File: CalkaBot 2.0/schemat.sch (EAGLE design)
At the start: 55 parts, among them IC1 TB6612FNG, IC2 LM339D, IC3 7806DT, Q1 16MHz, X1 MINI-USB-32005-301

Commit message: zmiana przycisków
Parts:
- removed BUT1, BUT2, BUT3: (no value), switch-omron:10-XX
- added SW2: (no value), special:SW_DIP-3
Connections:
- net GND: now also SW2.1, SW2.2, SW2.3; no longer BUT1.S, BUT1.S1, BUT2.S, BUT2.S1, BUT3.S, BUT3.S1
- net MISO: now also SW2.4; no longer BUT1.P, BUT1.P1
- net MOSI: now also SW2.5; no longer BUT2.P, BUT2.P1
- net SCK: now also SW2.6; no longer BUT3.P, BUT3.P1
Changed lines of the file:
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@@
 <?xml version="1.0" encoding="utf-8"?>
 <!DOCTYPE eagle SYSTEM "eagle.dtd">
-<eagle version="8.6.0">
+<eagle version="9.1.3">
 <drawing>
 <settings>
@@
 <part name="GND4" library="supply1" library_urn="urn:adsk.eagle:library:371" deviceset="GND" device=""/>
 <part name="R2" library="rcl" library_urn="urn:adsk.eagle:library:334" deviceset="R-EU_" device="R0805" package3d_urn="urn:adsk.eagle:package:23553/2" value="10k"/>
-<part name="BUT1" library="switch-omron" library_urn="urn:adsk.eagle:library:377" deviceset="10-XX" device="" package3d_urn="urn:adsk.eagle:package:27496/1"/>
 <part name="X1" library="con-cypressindustries" library_urn="urn:adsk.eagle:library:138" deviceset="MINI-USB-" device="32005-301" package3d_urn="urn:adsk.eagle:package:6446/1"/>
 <part name="R6" library="rcl" library_urn="urn:adsk.eagle:library:334" deviceset="R-EU_" device="R0805" package3d_urn="urn:adsk.eagle:package:23553/2" value="10k"/>
-<part name="BUT2" library="switch-omron" library_urn="urn:adsk.eagle:library:377" deviceset="10-XX" device="" package3d_urn="urn:adsk.eagle:package:27496/1"/>
 <part name="R9" library="rcl" library_urn="urn:adsk.eagle:library:334" deviceset="R-EU_" device="R0805" package3d_urn="urn:adsk.eagle:package:23553/2" value="10k"/>
-<part name="BUT3" library="switch-omron" library_urn="urn:adsk.eagle:library:377" deviceset="10-XX" device="" package3d_urn="urn:adsk.eagle:package:27496/1"/>
 <part name="IC3" library="linear3" deviceset="78*" device="DT" technology="06"/>
 <part name="GND7" library="supply1" library_urn="urn:adsk.eagle:library:371" deviceset="GND" device=""/>
@@
 <part name="JP2" library="pinhead" library_urn="urn:adsk.eagle:library:325" deviceset="PINHD-1X5" device="" package3d_urn="urn:adsk.eagle:package:22469/2"/>
 <part name="JP3" library="pinhead" library_urn="urn:adsk.eagle:library:325" deviceset="PINHD-1X5" device="" package3d_urn="urn:adsk.eagle:package:22469/2"/>
+<part name="SW2" library="special" library_urn="urn:adsk.eagle:library:367" deviceset="SW_DIP-3" device="" package3d_urn="urn:adsk.eagle:package:26663/2"/>
+<part name="GND22" library="supply1" library_urn="urn:adsk.eagle:library:371" deviceset="GND" device=""/>
 </parts>
 <sheets>
@@
 <instance part="GND4" gate="1" x="70.866" y="69.85"/>
 <instance part="R2" gate="G$1" x="-88.138" y="-0.508"/>
-<instance part="BUT1" gate="1" x="-88" y="-10.26" rot="R90"/>
 <instance part="X1" gate="G$1" x="-149.86" y="43.18" rot="R180"/>
 <instance part="R6" gate="G$1" x="-34.798" y="-0.508"/>
-<instance part="BUT2" gate="1" x="-34.66" y="-10.26" rot="R90"/>
 <instance part="R9" gate="G$1" x="21.082" y="-0.508"/>
-<instance part="BUT3" gate="1" x="21.22" y="-10.26" rot="R90"/>
 <instance part="IC3" gate="A1" x="68.58" y="124.46"/>
 <instance part="GND7" gate="1" x="68.58" y="111.76"/>
@@
 <instance part="JP2" gate="A" x="-119.38" y="25.4" rot="R270"/>
 <instance part="JP3" gate="A" x="-119.38" y="15.24" rot="R270"/>
+<instance part="SW2" gate="A" x="-27.94" y="-17.78" rot="R270"/>
+<instance part="GND22" gate="1" x="-27.94" y="-27.94"/>
 </instances>
 <busses>
@@
 <bus name="B$3">
 <segment>
-<wire x1="-111.76" y1="7.62" x2="-111.76" y2="-20.32" width="0.762" layer="92" style="shortdash"/>
-<wire x1="-111.76" y1="-20.32" x2="60.96" y2="-20.32" width="0.762" layer="92" style="shortdash"/>
-<wire x1="60.96" y1="-20.32" x2="60.96" y2="7.62" width="0.762" layer="92" style="shortdash"/>
+<wire x1="-111.76" y1="7.62" x2="-111.76" y2="-35.56" width="0.762" layer="92" style="shortdash"/>
+<wire x1="-111.76" y1="-35.56" x2="60.96" y2="-35.56" width="0.762" layer="92" style="shortdash"/>
+<wire x1="60.96" y1="-35.56" x2="60.96" y2="7.62" width="0.762" layer="92" style="shortdash"/>
 <wire x1="60.96" y1="7.62" x2="-111.76" y2="7.62" width="0.762" layer="92" style="shortdash"/>
 </segment>
@@
 </segment>
 <segment>
-<wire x1="-93.08" y1="-5.334" x2="-103.632" y2="-5.334" width="0.1524" layer="91"/>
-<junction x="-103.632" y="-5.334"/>
-<pinref part="BUT1" gate="1" pin="S"/>
-<pinref part="BUT1" gate="1" pin="S1"/>
-<wire x1="-93.08" y1="-10.26" x2="-93.08" y2="-7.72" width="0.1524" layer="91"/>
-<wire x1="-93.08" y1="-7.72" x2="-93.08" y2="-5.334" width="0.1524" layer="91"/>
-<junction x="-93.08" y="-7.72"/>
-<label x="-106.68" y="-5.08" size="1.016" layer="95"/>
-</segment>
-<segment>
 <pinref part="IC3" gate="A1" pin="GND"/>
 <wire x1="68.58" y1="116.84" x2="68.58" y2="114.3" width="0.1524" layer="91"/>
@@
 <wire x1="55.88" y1="137.16" x2="55.88" y2="132.08" width="0.1524" layer="91"/>
 <pinref part="GND18" gate="1" pin="GND"/>
-</segment>
-<segment>
-<wire x1="16.14" y1="-5.334" x2="5.588" y2="-5.334" width="0.1524" layer="91"/>
-<junction x="5.588" y="-5.334"/>
-<pinref part="BUT3" gate="1" pin="S"/>
-<pinref part="BUT3" gate="1" pin="S1"/>
-<wire x1="16.14" y1="-10.26" x2="16.14" y2="-7.72" width="0.1524" layer="91"/>
-<wire x1="16.14" y1="-7.72" x2="16.14" y2="-5.334" width="0.1524" layer="91"/>
-<junction x="16.14" y="-7.72"/>
-<label x="5.08" y="-5.08" size="1.016" layer="95"/>
-</segment>
-<segment>
-<wire x1="-39.74" y1="-5.334" x2="-50.292" y2="-5.334" width="0.1524" layer="91"/>
-<junction x="-50.292" y="-5.334"/>
-<pinref part="BUT2" gate="1" pin="S"/>
-<pinref part="BUT2" gate="1" pin="S1"/>
-<wire x1="-39.74" y1="-10.26" x2="-39.74" y2="-7.72" width="0.1524" layer="91"/>
-<wire x1="-39.74" y1="-7.72" x2="-39.74" y2="-5.334" width="0.1524" layer="91"/>
-<junction x="-39.74" y="-7.72"/>
-<label x="-53.34" y="-5.08" size="1.016" layer="95"/>
 </segment>
 <segment>
@@
 <label x="-46" y="44.5" size="1.778" layer="95"/>
 </segment>
+<segment>
+<pinref part="SW2" gate="A" pin="1"/>
+<pinref part="SW2" gate="A" pin="2"/>
+<wire x1="-30.48" y1="-25.4" x2="-27.94" y2="-25.4" width="0.1524" layer="91"/>
+<pinref part="SW2" gate="A" pin="3"/>
+<wire x1="-25.4" y1="-25.4" x2="-27.94" y2="-25.4" width="0.1524" layer="91"/>
+<junction x="-27.94" y="-25.4"/>
+<pinref part="GND22" gate="1" pin="GND"/>
+</segment>
 </net>
 <net name="D-" class="0">
@@
 <wire x1="-83.058" y1="-0.508" x2="-66.548" y2="-0.508" width="0.1524" layer="91"/>
 <junction x="-66.548" y="-0.508"/>
+<label x="-66.04" y="0" size="1.778" layer="95" xref="yes"/>
+<wire x1="-83.058" y1="-0.508" x2="-83.058" y2="-7.62" width="0.1524" layer="91"/>
+<wire x1="-83.058" y1="-7.62" x2="-33.02" y2="-7.62" width="0.1524" layer="91"/>
 <junction x="-83.058" y="-0.508"/>
-<wire x1="-83.058" y1="-5.334" x2="-83.058" y2="-0.508" width="0.1524" layer="91"/>
-<pinref part="BUT1" gate="1" pin="P1"/>
-<wire x1="-82.92" y1="-7.72" x2="-82.92" y2="-5.334" width="0.1524" layer="91"/>
-<wire x1="-82.92" y1="-5.334" x2="-83.058" y2="-5.334" width="0.1524" layer="91"/>
-<pinref part="BUT1" gate="1" pin="P"/>
-<wire x1="-82.92" y1="-10.26" x2="-82.92" y2="-7.72" width="0.1524" layer="91"/>
-<junction x="-82.92" y="-7.72"/>
-<label x="-66.04" y="0" size="1.778" layer="95" xref="yes"/>
+<pinref part="SW2" gate="A" pin="4"/>
+<wire x1="-33.02" y1="-7.62" x2="-30.48" y2="-7.62" width="0.1524" layer="91"/>
+<wire x1="-25.4" y1="-10.16" x2="-25.4" y2="-7.62" width="0.1524" layer="91"/>
+<wire x1="-25.4" y1="-7.62" x2="-30.48" y2="-7.62" width="0.1524" layer="91"/>
 </segment>
 </net>
@@
 <wire x1="-29.718" y1="-0.508" x2="-13.208" y2="-0.508" width="0.1524" layer="91"/>
 <junction x="-13.208" y="-0.508"/>
+<label x="-12.7" y="0" size="1.778" layer="95" xref="yes"/>
 <junction x="-29.718" y="-0.508"/>
-<wire x1="-29.718" y1="-5.334" x2="-29.718" y2="-0.508" width="0.1524" layer="91"/>
-<pinref part="BUT2" gate="1" pin="P1"/>
-<wire x1="-29.58" y1="-7.72" x2="-29.58" y2="-5.334" width="0.1524" layer="91"/>
-<wire x1="-29.58" y1="-5.334" x2="-29.718" y2="-5.334" width="0.1524" layer="91"/>
-<pinref part="BUT2" gate="1" pin="P"/>
-<wire x1="-29.58" y1="-10.26" x2="-29.58" y2="-7.72" width="0.1524" layer="91"/>
-<junction x="-29.58" y="-7.72"/>
-<label x="-12.7" y="0" size="1.778" layer="95" xref="yes"/>
+<pinref part="SW2" gate="A" pin="5"/>
+<wire x1="-29.718" y1="-0.508" x2="-27.94" y2="-0.508" width="0.1524" layer="91"/>
+<wire x1="-27.94" y1="-0.508" x2="-27.94" y2="-10.16" width="0.1524" layer="91"/>
 </segment>
 </net>
@@
 <wire x1="26.162" y1="-0.508" x2="42.672" y2="-0.508" width="0.1524" layer="91"/>
 <junction x="42.672" y="-0.508"/>
+<label x="43.18" y="0" size="1.778" layer="95" xref="yes"/>
+<wire x1="26.162" y1="-0.508" x2="25.4" y2="-0.508" width="0.1524" layer="91"/>
+<wire x1="25.4" y1="-0.508" x2="25.4" y2="-5.08" width="0.1524" layer="91"/>
 <junction x="26.162" y="-0.508"/>
-<wire x1="26.162" y1="-5.334" x2="26.162" y2="-0.508" width="0.1524" layer="91"/>
-<pinref part="BUT3" gate="1" pin="P1"/>
-<wire x1="26.3" y1="-7.72" x2="26.3" y2="-5.334" width="0.1524" layer="91"/>
-<wire x1="26.3" y1="-5.334" x2="26.162" y2="-5.334" width="0.1524" layer="91"/>
-<pinref part="BUT3" gate="1" pin="P"/>
-<wire x1="26.3" y1="-10.26" x2="26.3" y2="-7.72" width="0.1524" layer="91"/>
-<junction x="26.3" y="-7.72"/>
-<label x="43.18" y="0" size="1.778" layer="95" xref="yes"/>
+<wire x1="25.4" y1="-5.08" x2="-30.48" y2="-5.08" width="0.1524" layer="91"/>
+<pinref part="SW2" gate="A" pin="6"/>
+<wire x1="-30.48" y1="-10.16" x2="-30.48" y2="-5.08" width="0.1524" layer="91"/>
 </segment>
 </net>
@@
 </segment>
 </net>
+<net name="N$10" class="0">
+<segment>
+<wire x1="-29.58" y1="-5.334" x2="-29.718" y2="-5.334" width="0.1524" layer="91"/>
+</segment>
+</net>

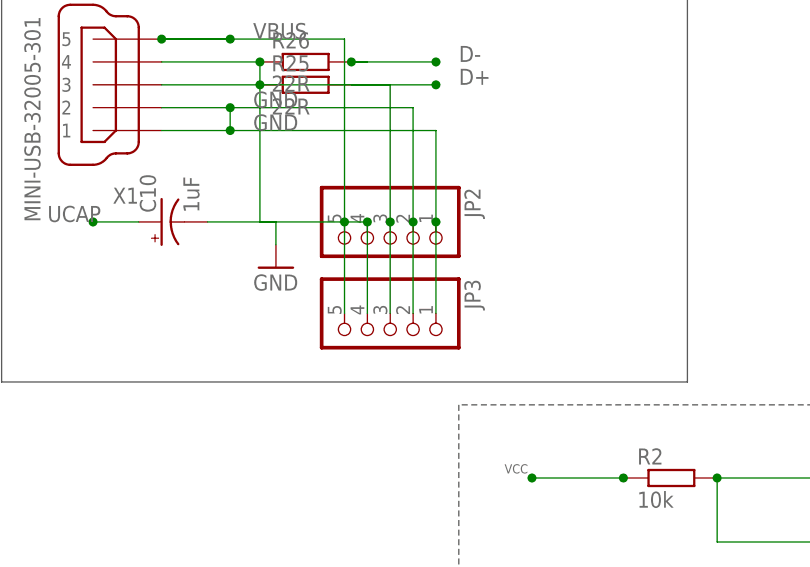
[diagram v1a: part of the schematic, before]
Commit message: połączono wszystkie vcc i gnd
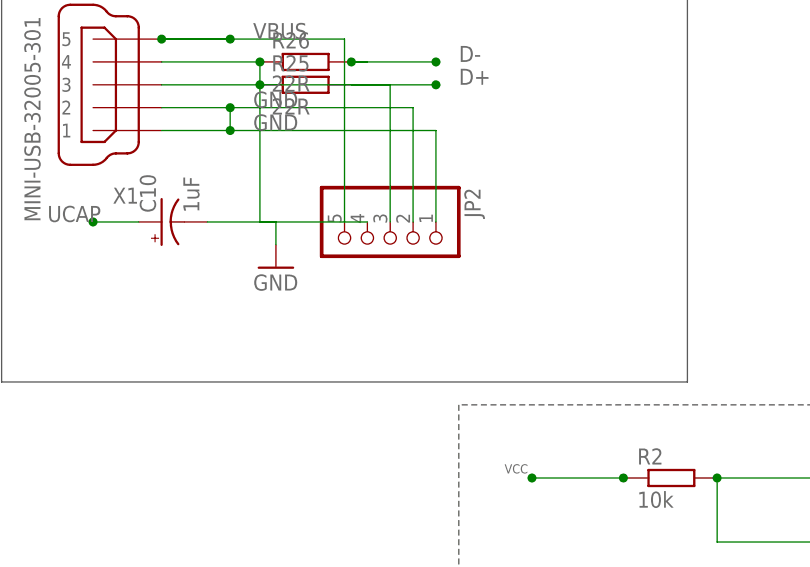
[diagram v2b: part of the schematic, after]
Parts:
- removed JP3: (no value), pinhead:PINHD-1X5
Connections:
- net GND: no longer JP3.1, JP3.2
- net N$12: no longer JP3.3
- net N$20: no longer JP3.4
- net VBUS: no longer JP3.5
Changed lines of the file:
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@@
 <part name="SW1" library="special" library_urn="urn:adsk.eagle:library:367" deviceset="SW_DIP-1" device="" package3d_urn="urn:adsk.eagle:package:26661/1"/>
 <part name="JP2" library="pinhead" library_urn="urn:adsk.eagle:library:325" deviceset="PINHD-1X5" device="" package3d_urn="urn:adsk.eagle:package:22469/2"/>
-<part name="JP3" library="pinhead" library_urn="urn:adsk.eagle:library:325" deviceset="PINHD-1X5" device="" package3d_urn="urn:adsk.eagle:package:22469/2"/>
 <part name="SW2" library="special" library_urn="urn:adsk.eagle:library:367" deviceset="SW_DIP-3" device="" package3d_urn="urn:adsk.eagle:package:26663/2"/>
 <part name="GND22" library="supply1" library_urn="urn:adsk.eagle:library:371" deviceset="GND" device=""/>
@@
 <instance part="SW1" gate="G$1" x="68.58" y="101.6" rot="R180"/>
 <instance part="JP2" gate="A" x="-119.38" y="25.4" rot="R270"/>
-<instance part="JP3" gate="A" x="-119.38" y="15.24" rot="R270"/>
 <instance part="SW2" gate="A" x="-27.94" y="-17.78" rot="R270"/>
 <instance part="GND22" gate="1" x="-27.94" y="-27.94"/>
@@
 <wire x1="-124.46" y1="48.26" x2="-124.46" y2="27.94" width="0.1524" layer="91"/>
 <junction x="-144.78" y="48.26"/>
-<pinref part="JP3" gate="A" pin="5"/>
-<wire x1="-124.46" y1="27.94" x2="-124.46" y2="17.78" width="0.1524" layer="91"/>
-<junction x="-124.46" y="27.94"/>
 </segment>
 </net>
@@
 <wire x1="-137.16" y1="38.1" x2="-114.3" y2="38.1" width="0.1524" layer="91"/>
 <wire x1="-114.3" y1="38.1" x2="-114.3" y2="27.94" width="0.1524" layer="91"/>
-<pinref part="JP3" gate="A" pin="2"/>
-<wire x1="-116.84" y1="27.94" x2="-116.84" y2="17.78" width="0.1524" layer="91"/>
-<junction x="-116.84" y="27.94"/>
-<pinref part="JP3" gate="A" pin="1"/>
-<wire x1="-114.3" y1="27.94" x2="-114.3" y2="17.78" width="0.1524" layer="91"/>
-<junction x="-114.3" y="27.94"/>
 </segment>
 <segment>
@@
 <wire x1="-119.38" y1="43.18" x2="-119.38" y2="27.94" width="0.1524" layer="91"/>
 <junction x="-133.858" y="43.18"/>
-<pinref part="JP3" gate="A" pin="3"/>
-<wire x1="-119.38" y1="27.94" x2="-119.38" y2="17.78" width="0.1524" layer="91"/>
-<junction x="-119.38" y="27.94"/>
 </segment>
 </net>
@@
 <wire x1="-133.858" y1="27.94" x2="-121.92" y2="27.94" width="0.1524" layer="91"/>
 <junction x="-133.858" y="45.72"/>
-<pinref part="JP3" gate="A" pin="4"/>
-<wire x1="-121.92" y1="27.94" x2="-121.92" y2="17.78" width="0.1524" layer="91"/>
-<junction x="-121.92" y="27.94"/>
-</segment>
-</net>
+</segment>
+</net>
